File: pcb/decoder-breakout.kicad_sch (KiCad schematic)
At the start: 18 parts, among them J1 SM04B-SRSS-TB_LF__SN_, J2 SM04B-SRSS-TB_LF__SN_, J3 TBL009-254-08GY-2GY, Q1 BSS138, Q2 BSS138, U1 LS7866-S

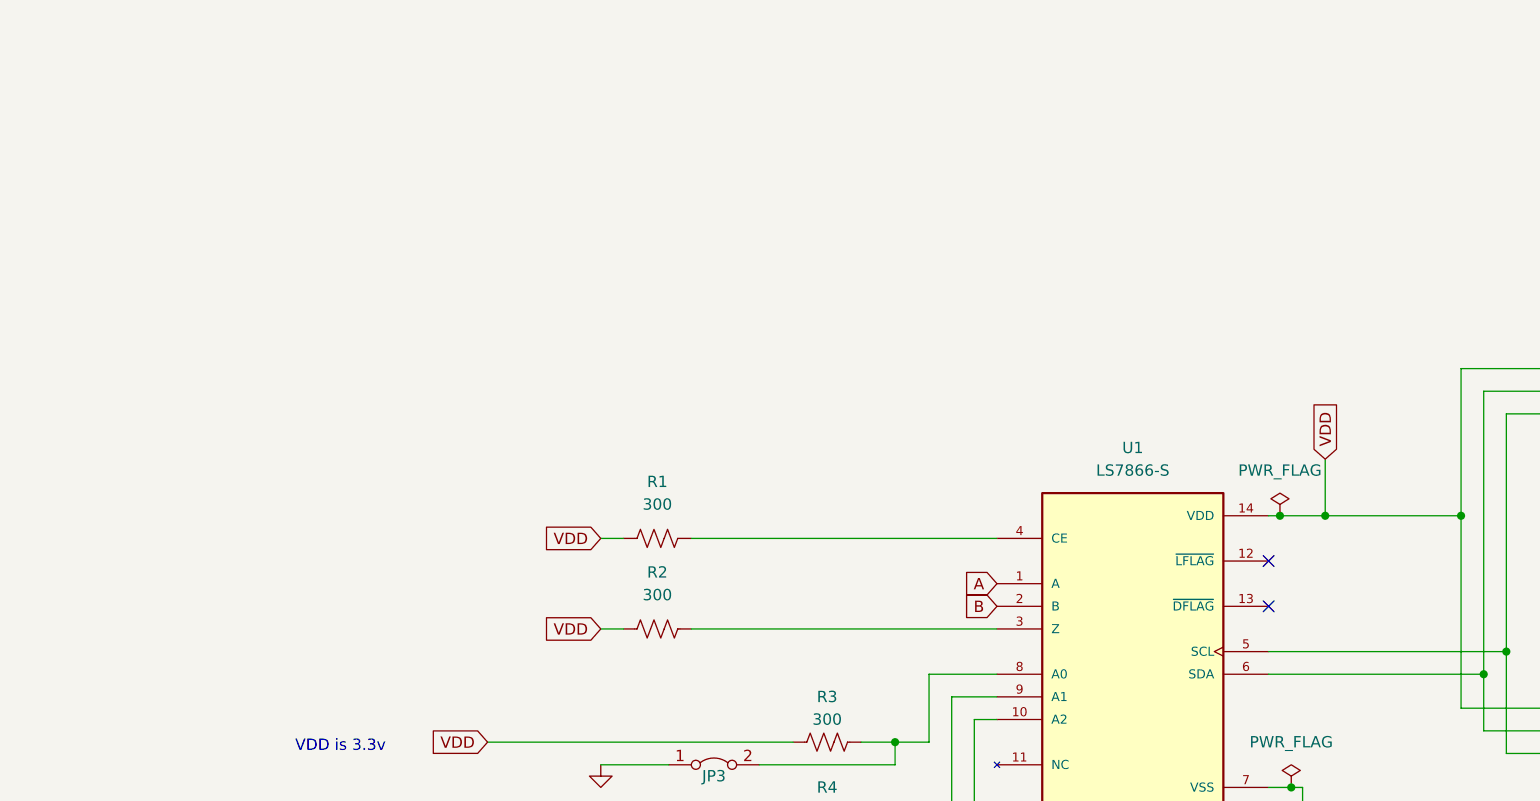
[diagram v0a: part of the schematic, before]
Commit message: add decoupling cap, mounting holes and board edges
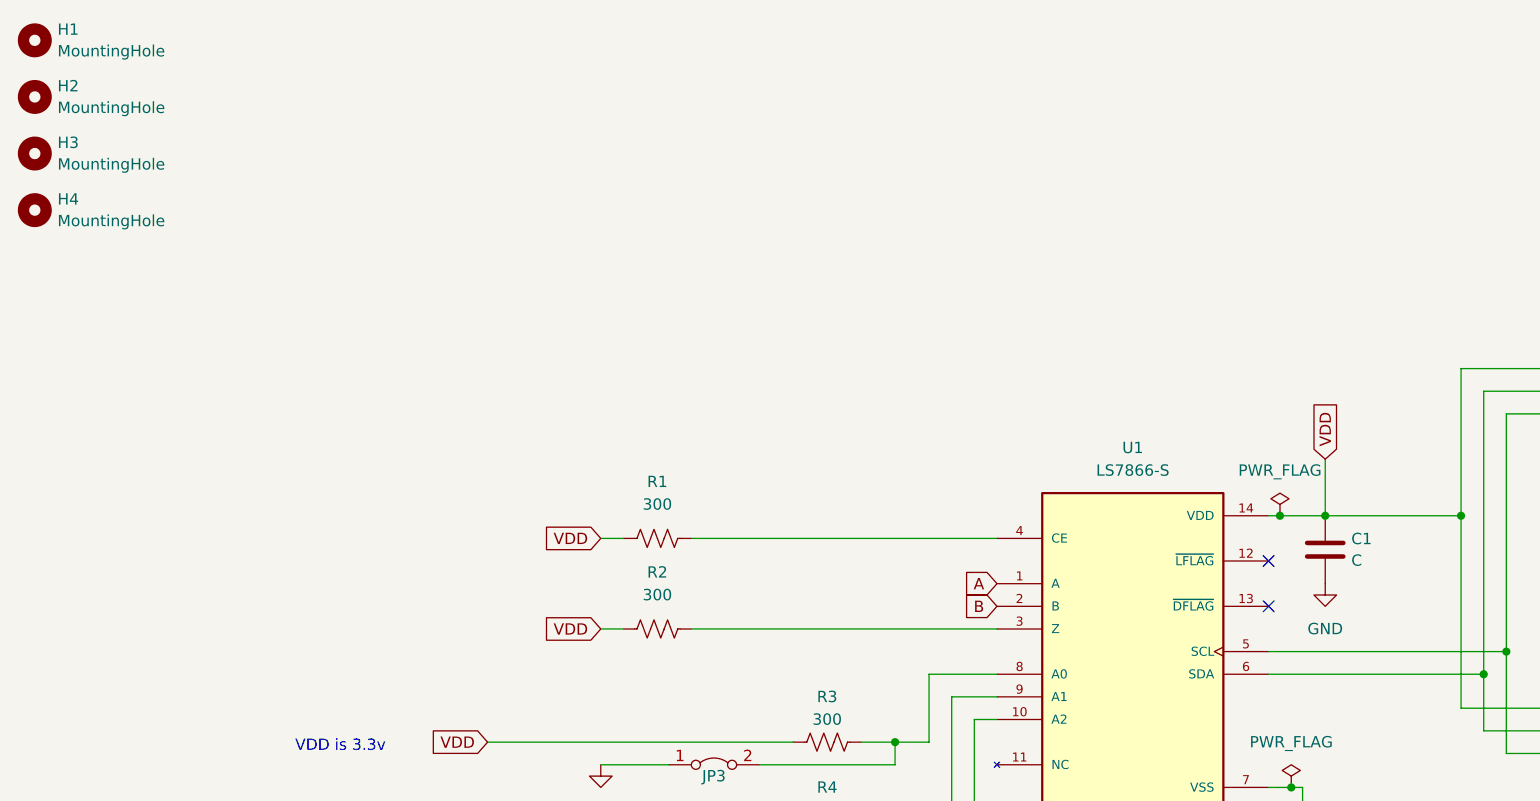
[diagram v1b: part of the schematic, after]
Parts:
- added C1: C, Capacitor_SMD:C_1812_4532Metric_Pad1.57x3.40mm_HandSolder, symbol Device:C
- added H1, H2, H3, H4: MountingHole, MountingHole:MountingHole_2.5mm_Pad, symbol Mechanical:MountingHole
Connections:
- net GND: now also C1.2
- net VDD: now also C1.1
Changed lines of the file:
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@@
+    )
+  )
+  (symbol (lib_id "Mechanical:MountingHole") (at 22.86 22.86 0) (unit 1)
+    (in_bom yes) (on_board yes) (dnp no) (fields_autoplaced)
+    (property "Reference" "H1" (at 25.4 21.6479 0)
+      (effects (font (size 1.27 1.27)) (justify left))
+    )
+    (property "Value" "MountingHole" (at 25.4 24.0721 0)
+      (effects (font (size 1.27 1.27)) (justify left))
+    )
+    (property "Footprint" "MountingHole:MountingHole_2.5mm_Pad" (at 22.86 22.86 0)
+      (effects (font (size 1.27 1.27)) hide)
+    )
+    (property "Datasheet" "~" (at 22.86 22.86 0)
+      (effects (font (size 1.27 1.27)) hide)
+    )
+    (instances
+      (project "decoder-breakout"
+        (path "/1a0ebad1-ea8c-4043-8a0c-94ccddf3b0fc"
+          (reference "H1") (unit 1)
+        )
+      )
     )
   )
@@
         (path "/1a0ebad1-ea8c-4043-8a0c-94ccddf3b0fc"
           (reference "#FLG01") (unit 1)
+        )
+      )
+    )
+  )
+  (symbol (lib_id "Mechanical:MountingHole") (at 22.86 41.91 0) (unit 1)
+    (in_bom yes) (on_board yes) (dnp no) (fields_autoplaced)
+    (property "Reference" "H4" (at 25.4 40.6979 0)
+      (effects (font (size 1.27 1.27)) (justify left))
+    )
+    (property "Value" "MountingHole" (at 25.4 43.1221 0)
+      (effects (font (size 1.27 1.27)) (justify left))
+    )
+    (property "Footprint" "MountingHole:MountingHole_2.5mm_Pad" (at 22.86 41.91 0)
+      (effects (font (size 1.27 1.27)) hide)
+    )
+    (property "Datasheet" "~" (at 22.86 41.91 0)
+      (effects (font (size 1.27 1.27)) hide)
+    )
+    (instances
+      (project "decoder-breakout"
+        (path "/1a0ebad1-ea8c-4043-8a0c-94ccddf3b0fc"
+          (reference "H4") (unit 1)
         )
       )
@@
     )
   )
+  (symbol (lib_id "Device:C") (at 167.64 80.01 0) (unit 1)
+    (in_bom yes) (on_board yes) (dnp no) (fields_autoplaced)
+    (property "Reference" "C1" (at 170.561 78.7979 0)
+      (effects (font (size 1.27 1.27)) (justify left))
+    )
+    (property "Value" "C" (at 170.561 81.2221 0)
+      (effects (font (size 1.27 1.27)) (justify left))
+    )
+    (property "Footprint" "Capacitor_SMD:C_1812_4532Metric_Pad1.57x3.40mm_HandSolder" (at 168.6052 83.82 0)
+      (effects (font (size 1.27 1.27)) hide)
+    )
+    (property "Datasheet" "CHV1812N250105MXT" (at 167.64 80.01 0)
+      (effects (font (size 1.27 1.27)) hide)
+    )
+    (pin "2")
+    (pin "1")
+    (instances
+      (project "decoder-breakout"
+        (path "/1a0ebad1-ea8c-4043-8a0c-94ccddf3b0fc"
+          (reference "C1") (unit 1)
+        )
+      )
+    )
+  )
+  (symbol (lib_id "Mechanical:MountingHole") (at 22.86 29.21 0) (unit 1)
+    (in_bom yes) (on_board yes) (dnp no) (fields_autoplaced)
+    (property "Reference" "H2" (at 25.4 27.9979 0)
+      (effects (font (size 1.27 1.27)) (justify left))
+    )
+    (property "Value" "MountingHole" (at 25.4 30.4221 0)
+      (effects (font (size 1.27 1.27)) (justify left))
+    )
+    (property "Footprint" "MountingHole:MountingHole_2.5mm_Pad" (at 22.86 29.21 0)
+      (effects (font (size 1.27 1.27)) hide)
+    )
+    (property "Datasheet" "~" (at 22.86 29.21 0)
+      (effects (font (size 1.27 1.27)) hide)
+    )
+    (instances
+      (project "decoder-breakout"
+        (path "/1a0ebad1-ea8c-4043-8a0c-94ccddf3b0fc"
+          (reference "H2") (unit 1)
+        )
+      )
+    )
+  )
   (symbol (lib_id "Transistor_FET:BSS138") (at 127 168.91 270) (unit 1)
     (in_bom yes) (on_board yes) (dnp no) (fields_autoplaced)
@@
         (path "/1a0ebad1-ea8c-4043-8a0c-94ccddf3b0fc"
           (reference "Q1") (unit 1)
+        )
+      )
+    )
+  )
+  (symbol (lib_id "power:GND") (at 167.64 83.82 0) (unit 1)
+    (in_bom yes) (on_board yes) (dnp no) (fields_autoplaced)
+    (property "Reference" "#PWR06" (at 167.64 90.17 0)
+      (effects (font (size 1.27 1.27)) hide)
+    )
+    (property "Value" "GND" (at 167.64 88.9 0)
+      (effects (font (size 1.27 1.27)))
+    )
+    (property "Footprint" "" (at 167.64 83.82 0)
+      (effects (font (size 1.27 1.27)) hide)
+    )
+    (property "Datasheet" "" (at 167.64 83.82 0)
+      (effects (font (size 1.27 1.27)) hide)
+    )
+    (pin "1")
+    (instances
+      (project "decoder-breakout"
+        (path "/1a0ebad1-ea8c-4043-8a0c-94ccddf3b0fc"
+          (reference "#PWR06") (unit 1)
         )
       )
@@
         )
       )
+    )
+  )
+  (symbol (lib_id "Mechanical:MountingHole") (at 22.86 35.56 0) (unit 1)
+    (in_bom yes) (on_board yes) (dnp no) (fields_autoplaced)
+    (property "Reference" "H3" (at 25.4 34.3479 0)
+      (effects (font (size 1.27 1.27)) (justify left))
+    )
+    (property "Value" "MountingHole" (at 25.4 36.7721 0)
+      (effects (font (size 1.27 1.27)) (justify left))
+    )
+    (property "Footprint" "MountingHole:MountingHole_2.5mm_Pad" (at 22.86 35.56 0)
+      (effects (font (size 1.27 1.27)) hide)
+    )
+    (property "Datasheet" "~" (at 22.86 35.56 0)
+      (effects (font (size 1.27 1.27)) hide)
+    )
+    (instances
+      (project "decoder-breakout"
+        (path "/1a0ebad1-ea8c-4043-8a0c-94ccddf3b0fc"
+          (reference "H3") (unit 1)
+        )
+      )

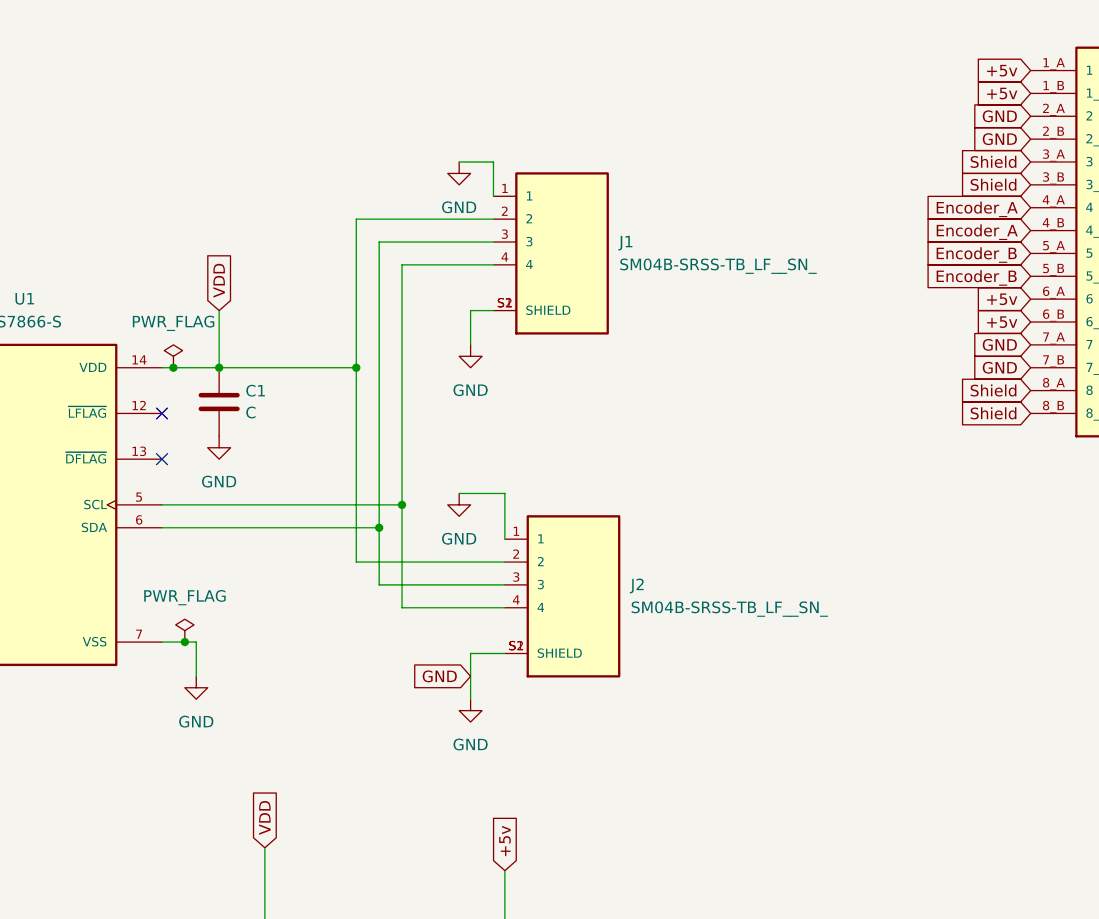
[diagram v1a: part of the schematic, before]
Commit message: Adjust PCB design, skip I2C reserved addresses, tweak delays
Move, add junctions; adjust wires; update symbols, labels

summary of diff --git  a/pcb/decoder-breakout.kicad_sch b/pcb/decoder-breakout.kicad_sch

- Move some junctions to new coordinates on the schematic
- Add new junctions with unique UUIDs
- Adjust wire connections to match new junction positions
- Remove a junction and its associated wires
- Update global label "GND" with new position and intersheet reference coordinates
- Adjust symbols for "power:GND" with updated positions
- Update "SM04B-SRSS-TB_LF__SN_" symbol with new position and properties including reference, footprint, description, and manufacturer details
- Insert "Device:R_US" symbols with properties for "R11" and "R10" including reference, value, and footprint details

Skip 0-7 I2C addresses, explain why, reference issue, adjust delays

summary of diff --git  a/src/photon2addressScanner/src/L07_00_I2CScanner.cpp b/src/photon2addressScanner/src/L07_00_I2CScanner.cpp

- Change I2C scan range to exclude addresses 0-7 as they are reserved for special purposes
- Add comments to explain why addresses 0-7 are skipped during scanning
- Include a reference to an Arduino GitHub issue discussing reserved I2C addresses
- Ensure delay(1) is called after every address scan, not only when an address is found
- Increase the delay after completing the scan of all addresses to 5000 milliseconds
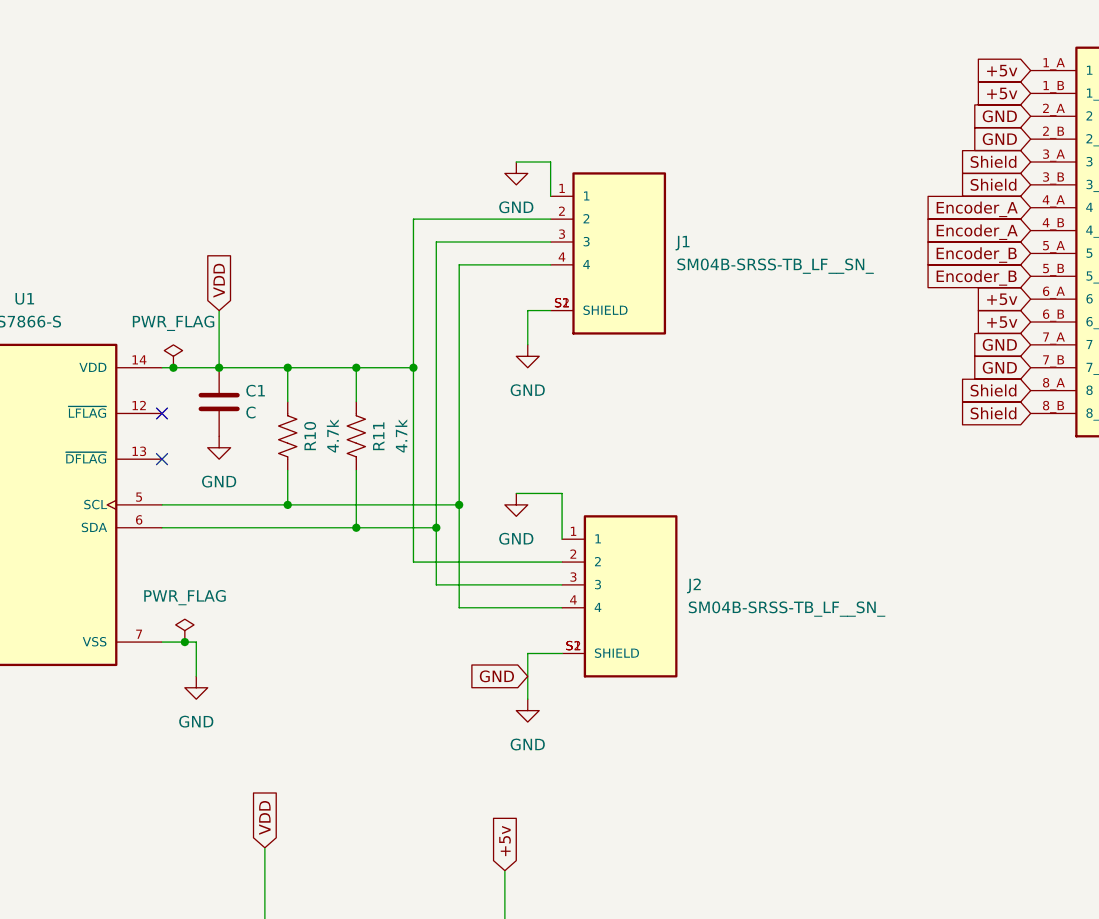
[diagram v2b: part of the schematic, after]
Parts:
- added R10, R11: 4.7k, Resistor_SMD:R_2010_5025Metric_Pad1.40x2.65mm_HandSolder, symbol Device:R_US
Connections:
- net VDD: now also R10.1, R11.1
- net at J1.4, J2.4, U1.5 (SCL): now also R10.2
- net at J1.3, J2.3, U1.6 (SDA): now also R11.2
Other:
- moved on the sheet: J1, J2
